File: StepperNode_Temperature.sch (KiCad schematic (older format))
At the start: 0 parts

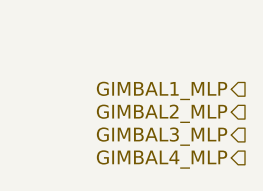
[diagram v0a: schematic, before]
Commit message: Added sheet for Stepper Motor RTD temp sensors.
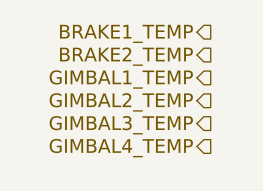
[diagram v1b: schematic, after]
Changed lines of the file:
@@
 $Descr A3 16535 11693
 encoding utf-8
-Sheet 10 17
-Title "Gimbal 4-20ma MLP Interface"
+Sheet 17 17
+Title "Stepper Motor Temperature Interface"
 Date ""
 Rev "1"
@@
 Comment4 ""
 $EndDescr
-Text HLabel 1700 1250 0    60   Output ~ 0
-GIMBAL1_MLP
-Text HLabel 1700 1350 0    60   Output ~ 0
-GIMBAL2_MLP
-Text HLabel 1700 1450 0    60   Output ~ 0
-GIMBAL3_MLP
-Text HLabel 1700 1550 0    60   Output ~ 0
-GIMBAL4_MLP
+Text HLabel 1550 1000 0    60   Output ~ 0
+BRAKE1_TEMP
+Text HLabel 1550 1100 0    60   Output ~ 0
+BRAKE2_TEMP
+Text HLabel 1550 1200 0    60   Output ~ 0
+GIMBAL1_TEMP
+Text HLabel 1550 1300 0    60   Output ~ 0
+GIMBAL2_TEMP
+Text HLabel 1550 1400 0    60   Output ~ 0
+GIMBAL3_TEMP
+Text HLabel 1550 1500 0    60   Output ~ 0
+GIMBAL4_TEMP
 $EndSCHEMATC

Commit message: Update Stepper Temp Sensor Interface
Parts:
- added C? (x6): 100nF, symbol C
- added C? (x6): 1uF, symbol C
- added D? (x6): 1N4148, symbol D
- added P? (x2): CONN_01X08_2MNT, symbol CONN_01X08_2MNT
- added U? (x6): RCV420JP, symbol RCV420JP
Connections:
- net labels added: +24V_A, BRAKE_T1_420MA, BRAKE_T2_420MA, BRAKE_T3_420MA, BRAKE_T4_420MA, GIMBAL_T1_420MA, GIMBAL_T2_420MA, GIMBAL_T3_420MA, GIMBAL_T4_420MA, GNDA
- wire segments 0 -> 60
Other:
- note added: "4-20mA for Brake and\nGimbal Temp"
- note added: "4-20mA for Gimbal Temp"
- note added: "Original Author: SafetyLok"
- note added: "rLoop - Stepper Node\n4-20mA Temp Sensor IF\n"

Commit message: Remove Gimbal Functions
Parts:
- removed C? (x4): 100nF, symbol C
- removed C? (x4): 1uF, symbol C
- removed D? (x4): 1N4148, symbol D
- removed P?: CONN_01X08_2MNT, symbol CONN_01X08_2MNT
- removed U? (x4): RCV420JP, symbol RCV420JP
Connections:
- net labels removed: GIMBAL1_TEMP, GIMBAL2_TEMP, GIMBAL3_TEMP, GIMBAL4_TEMP, GIMBAL_T1_420MA, GIMBAL_T2_420MA, GIMBAL_T3_420MA, GIMBAL_T4_420MA
- wire segments 60 -> 20
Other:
- note removed: "4-20mA for Brake and\nGimbal Temp"
- moved on the sheet: U?

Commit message: Update DAC's and routed gimbal position to MCU direct.
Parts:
- removed C? (x2): 100nF, symbol C
- removed C? (x2): 1uF, symbol C
- removed U? (x2): RCV420JP, symbol RCV420JP
- added C? (x2): C_100nF_50V, RLOOP_FOOTPRINTS:rLoop_C_0603, symbol C_100nF_50V
- added C? (x2): C_1uF_50V, RLOOP_FOOTPRINTS:rLoop_C_0603, symbol C_1uF_50V
- added U? (x2): RCV420JP, symbol RCV420JP
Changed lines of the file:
@@
 Original Author: SafetyLok
-$Comp
-L RCV420JP U?
-U 1 1 575668D5
-P 6900 2850
-F 0 "U?" H 6950 2950 60  0000 C CNN
-F 1 "RCV420JP" H 6900 1650 60  0000 C CNN
-F 2 "" H 6900 2850 60  0000 C CNN
-F 3 "" H 6900 2850 60  0000 C CNN
-	1    6900 2850
-	-1   0    0    -1
-$EndComp
 $Comp
 L +24V_A #PWR?
@@
 	5600 3350 5400 3350
 $Comp
-L C C?
-U 1 1 575669A6
-P 5150 4050
-F 0 "C?" H 5175 4150 50  0000 L CNN
-F 1 "100nF" H 5175 3950 50  0000 L CNN
-F 2 "" H 5188 3900 50  0000 C CNN
-F 3 "" H 5150 4050 50  0000 C CNN
-	1    5150 4050
-	1    0    0    -1
-$EndComp
-$Comp
-L C C?
-U 1 1 57566A33
-P 5450 4050
-F 0 "C?" H 5475 4150 50  0000 L CNN
-F 1 "1uF" H 5475 3950 50  0000 L CNN
-F 2 "" H 5488 3900 50  0000 C CNN
-F 3 "" H 5450 4050 50  0000 C CNN
-	1    5450 4050
-	1    0    0    -1
-$EndComp
-$Comp
 L GNDA #PWR?
 U 1 1 57566A6C
@@
 $Comp
 L GNDA #PWR?
-U 1 1 57566A84
-P 5150 4200
-F 0 "#PWR?" H 5150 3950 50  0001 C CNN
-F 1 "GNDA" H 5150 4050 50  0000 C CNN
-F 2 "" H 5150 4200 50  0000 C CNN
-F 3 "" H 5150 4200 50  0000 C CNN
-	1    5150 4200
-	1    0    0    -1
-$EndComp
-$Comp
-L GNDA #PWR?
 U 1 1 57566A8F
-P 5450 4200
-F 0 "#PWR?" H 5450 3950 50  0001 C CNN
-F 1 "GNDA" H 5450 4050 50  0000 C CNN
-F 2 "" H 5450 4200 50  0000 C CNN
-F 3 "" H 5450 4200 50  0000 C CNN
-	1    5450 4200
-	1    0    0    -1
-$EndComp
-$Comp
-L +24V_A #PWR?
-U 1 1 57566A9A
-P 5150 3900
-F 0 "#PWR?" H 5150 3750 50  0001 C CNN
-F 1 "+24V_A" H 5150 4040 50  0000 C CNN
-F 2 "" H 5150 3900 60  0000 C CNN
-F 3 "" H 5150 3900 60  0000 C CNN
-	1    5150 3900
-	-1   0    0    -1
+P 5100 4200
+F 0 "#PWR?" H 5100 3950 50  0001 C CNN
+F 1 "GNDA" H 5100 4050 50  0000 C CNN
+F 2 "" H 5100 4200 50  0000 C CNN
+F 3 "" H 5100 4200 50  0000 C CNN
+	1    5100 4200
+	1    0    0    -1
 $EndComp
 $Comp
 L +24V_A #PWR?
 U 1 1 57566AA5
-P 5450 3900
-F 0 "#PWR?" H 5450 3750 50  0001 C CNN
-F 1 "+24V_A" H 5450 4040 50  0000 C CNN
-F 2 "" H 5450 3900 60  0000 C CNN
-F 3 "" H 5450 3900 60  0000 C CNN
-	1    5450 3900
+P 5100 3900
+F 0 "#PWR?" H 5100 3750 50  0001 C CNN
+F 1 "+24V_A" H 5100 4040 50  0000 C CNN
+F 2 "" H 5100 3900 60  0000 C CNN
+F 3 "" H 5100 3900 60  0000 C CNN
+	1    5100 3900
 	-1   0    0    -1
 $EndComp
@@
 BRAKE2_TEMP
 $Comp
-L RCV420JP U?
-U 1 1 57568DC3
-P 6900 5200
-F 0 "U?" H 6950 5300 60  0000 C CNN
-F 1 "RCV420JP" H 6900 4000 60  0000 C CNN
-F 2 "" H 6900 5200 60  0000 C CNN
-F 3 "" H 6900 5200 60  0000 C CNN
-	1    6900 5200
-	-1   0    0    -1
-$EndComp
-$Comp
 L +24V_A #PWR?
 U 1 1 57568DC9
@@
 	5600 5700 5400 5700
 $Comp
-L C C?
-U 1 1 57568DD2
-P 5150 6400
-F 0 "C?" H 5175 6500 50  0000 L CNN
-F 1 "100nF" H 5175 6300 50  0000 L CNN
-F 2 "" H 5188 6250 50  0000 C CNN
-F 3 "" H 5150 6400 50  0000 C CNN
-	1    5150 6400
-	1    0    0    -1
-$EndComp
-$Comp
-L C C?
-U 1 1 57568DD8
-P 5450 6400
-F 0 "C?" H 5475 6500 50  0000 L CNN
-F 1 "1uF" H 5475 6300 50  0000 L CNN
-F 2 "" H 5488 6250 50  0000 C CNN
-F 3 "" H 5450 6400 50  0000 C CNN
-	1    5450 6400
-	1    0    0    -1
-$EndComp
-$Comp
 L GNDA #PWR?
 U 1 1 57568DDE
@@
 	1    6550 6600
 	1    0    0    -1
-$EndComp
-$Comp
-L GNDA #PWR?
-U 1 1 57568DE4
-P 5150 6550
-F 0 "#PWR?" H 5150 6300 50  0001 C CNN
-F 1 "GNDA" H 5150 6400 50  0000 C CNN
-F 2 "" H 5150 6550 50  0000 C CNN
-F 3 "" H 5150 6550 50  0000 C CNN
-	1    5150 6550
-	1    0    0    -1
-$EndComp
-$Comp
-L GNDA #PWR?
-U 1 1 57568DEA
-P 5450 6550
-F 0 "#PWR?" H 5450 6300 50  0001 C CNN
-F 1 "GNDA" H 5450 6400 50  0000 C CNN
-F 2 "" H 5450 6550 50  0000 C CNN
-F 3 "" H 5450 6550 50  0000 C CNN
-	1    5450 6550
-	1    0    0    -1
-$EndComp
-$Comp
-L +24V_A #PWR?
-U 1 1 57568DF0
-P 5150 6250
-F 0 "#PWR?" H 5150 6100 50  0001 C CNN
-F 1 "+24V_A" H 5150 6390 50  0000 C CNN
-F 2 "" H 5150 6250 60  0000 C CNN
-F 3 "" H 5150 6250 60  0000 C CNN
-	1    5150 6250
-	-1   0    0    -1
-$EndComp
-$Comp
-L +24V_A #PWR?
-U 1 1 57568DF6
-P 5450 6250
-F 0 "#PWR?" H 5450 6100 50  0001 C CNN
-F 1 "+24V_A" H 5450 6390 50  0000 C CNN
-F 2 "" H 5450 6250 60  0000 C CNN
-F 3 "" H 5450 6250 60  0000 C CNN
-	1    5450 6250
-	-1   0    0    -1
 $EndComp
 Wire Wire Line
@@
 Text Label 7250 5900 0    60   ~ 0
 BRAKE_T2_420MA
+$Comp
+L RCV420JP U?
+U 1 1 575A3554
+P 6900 2850
+F 0 "U?" H 6950 2950 60  0000 C CNN
+F 1 "RCV420JP" H 6900 1650 60  0000 C CNN
+F 2 "" H 6900 2850 60  0000 C CNN
+F 3 "" H 6900 2850 60  0000 C CNN
+	1    6900 2850
+	-1   0    0    -1
+$EndComp
+$Comp
+L RCV420JP U?
+U 1 1 575A3707
+P 6900 5200
+F 0 "U?" H 6950 5300 60  0000 C CNN
+F 1 "RCV420JP" H 6900 4000 60  0000 C CNN
+F 2 "" H 6900 5200 60  0000 C CNN
+F 3 "" H 6900 5200 60  0000 C CNN
+	1    6900 5200
+	-1   0    0    -1
+$EndComp
+$Comp
+L GNDA #PWR?
+U 1 1 575A39DB
+P 4400 4200
+F 0 "#PWR?" H 4400 3950 50  0001 C CNN
+F 1 "GNDA" H 4400 4050 50  0000 C CNN
+F 2 "" H 4400 4200 50  0000 C CNN
+F 3 "" H 4400 4200 50  0000 C CNN
+	1    4400 4200
+	1    0    0    -1
+$EndComp
+$Comp
+L +24V_A #PWR?
+U 1 1 575A39E1
+P 4400 3900
+F 0 "#PWR?" H 4400 3750 50  0001 C CNN
+F 1 "+24V_A" H 4400 4040 50  0000 C CNN
+F 2 "" H 4400 3900 60  0000 C CNN
+F 3 "" H 4400 3900 60  0000 C CNN
+	1    4400 3900
+	-1   0    0    -1
+$EndComp
+$Comp
+L C_100nF_50V C?
+U 1 1 575A39E7
+P 4400 4050
+F 0 "C?" H 4425 4150 50  0000 L CNN
+F 1 "C_100nF_50V" H 4425 3950 50  0000 L CNN
+F 2 "RLOOP_FOOTPRINTS:rLoop_C_0603" H 4438 3900 50  0001 C CNN
+F 3 "" H 4400 4050 50  0000 C CNN
+	1    4400 4050
+	1    0    0    -1
+$EndComp
+$Comp
+L C_1uF_50V C?
+U 1 1 575A3AB4
+P 5100 4050
+F 0 "C?" H 5125 4150 50  0000 L CNN
+F 1 "C_1uF_50V" H 5125 3950 50  0000 L CNN
+F 2 "RLOOP_FOOTPRINTS:rLoop_C_0603" H 5138 3900 50  0001 C CNN
+F 3 "" H 5100 4050 50  0000 C CNN
+	1    5100 4050
+	1    0    0    -1
+$EndComp
+$Comp
+L GNDA #PWR?
+U 1 1 575A3CB4
+P 5200 6600
+F 0 "#PWR?" H 5200 6350 50  0001 C CNN
+F 1 "GNDA" H 5200 6450 50  0000 C CNN
+F 2 "" H 5200 6600 50  0000 C CNN
+F 3 "" H 5200 6600 50  0000 C CNN
+	1    5200 6600
+	1    0    0    -1
+$EndComp
+$Comp
+L +24V_A #PWR?
+U 1 1 575A3CBA
+P 5200 6300
+F 0 "#PWR?" H 5200 6150 50  0001 C CNN
+F 1 "+24V_A" H 5200 6440 50  0000 C CNN
+F 2 "" H 5200 6300 60  0000 C CNN
+F 3 "" H 5200 6300 60  0000 C CNN
+	1    5200 6300
+	-1   0    0    -1
+$EndComp
+$Comp
+L GNDA #PWR?
+U 1 1 575A3CC0
+P 4500 6600
+F 0 "#PWR?" H 4500 6350 50  0001 C CNN
+F 1 "GNDA" H 4500 6450 50  0000 C CNN
+F 2 "" H 4500 6600 50  0000 C CNN
+F 3 "" H 4500 6600 50  0000 C CNN
+	1    4500 6600
+	1    0    0    -1
+$EndComp
+$Comp
+L +24V_A #PWR?
+U 1 1 575A3CC6
+P 4500 6300
+F 0 "#PWR?" H 4500 6150 50  0001 C CNN
+F 1 "+24V_A" H 4500 6440 50  0000 C CNN
+F 2 "" H 4500 6300 60  0000 C CNN
+F 3 "" H 4500 6300 60  0000 C CNN
+	1    4500 6300
+	-1   0    0    -1
+$EndComp
+$Comp
+L C_100nF_50V C?
+U 1 1 575A3CCC
+P 4500 6450
+F 0 "C?" H 4525 6550 50  0000 L CNN
+F 1 "C_100nF_50V" H 4525 6350 50  0000 L CNN
+F 2 "RLOOP_FOOTPRINTS:rLoop_C_0603" H 4538 6300 50  0001 C CNN
+F 3 "" H 4500 6450 50  0000 C CNN
+	1    4500 6450
+	1    0    0    -1
+$EndComp
+$Comp
+L C_1uF_50V C?
+U 1 1 575A3CD2
+P 5200 6450
+F 0 "C?" H 5225 6550 50  0000 L CNN
+F 1 "C_1uF_50V" H 5225 6350 50  0000 L CNN
+F 2 "RLOOP_FOOTPRINTS:rLoop_C_0603" H 5238 6300 50  0001 C CNN
+F 3 "" H 5200 6450 50  0000 C CNN
+	1    5200 6450
+	1    0    0    -1
+$EndComp
 $EndSCHEMATC

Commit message: First Revision -
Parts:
- removed D? (x2): 1N4148, symbol D
- removed P?: CONN_01X08_2MNT, symbol CONN_01X08_2MNT
- removed U? (x2): RCV420JP, symbol RCV420JP
- added D7, D8: BAS16,215, RLOOP_FOOTPRINTS:rLoop_SOT23, symbol BAS16,215
- added P13: TE_640456-8, RLOOP_FOOTPRINTS:rLoop_TE640456-8, symbol TE_640456-8
- added U23, U24: RCV420JP, RLOOP_FOOTPRINTS:rLoop_DIP16, symbol RCV420JP
- gave numbers to parts that had none: 4
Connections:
- net labels removed: BRAKE_T3_420MA, BRAKE_T4_420MA
- wire segments 20 -> 23

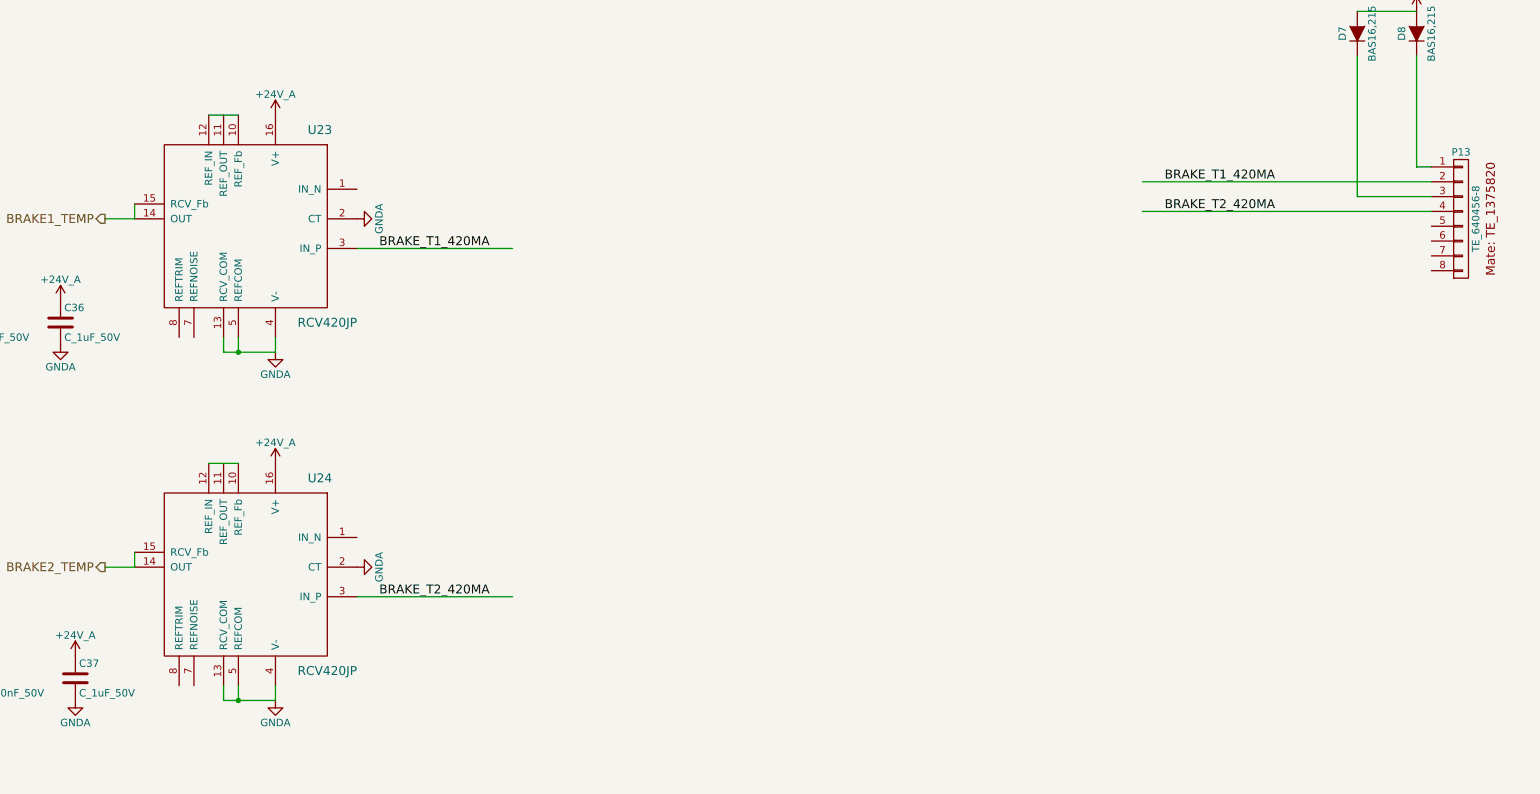
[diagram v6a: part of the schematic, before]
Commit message: Fix most ERC warnings (non-connected pins, etc)
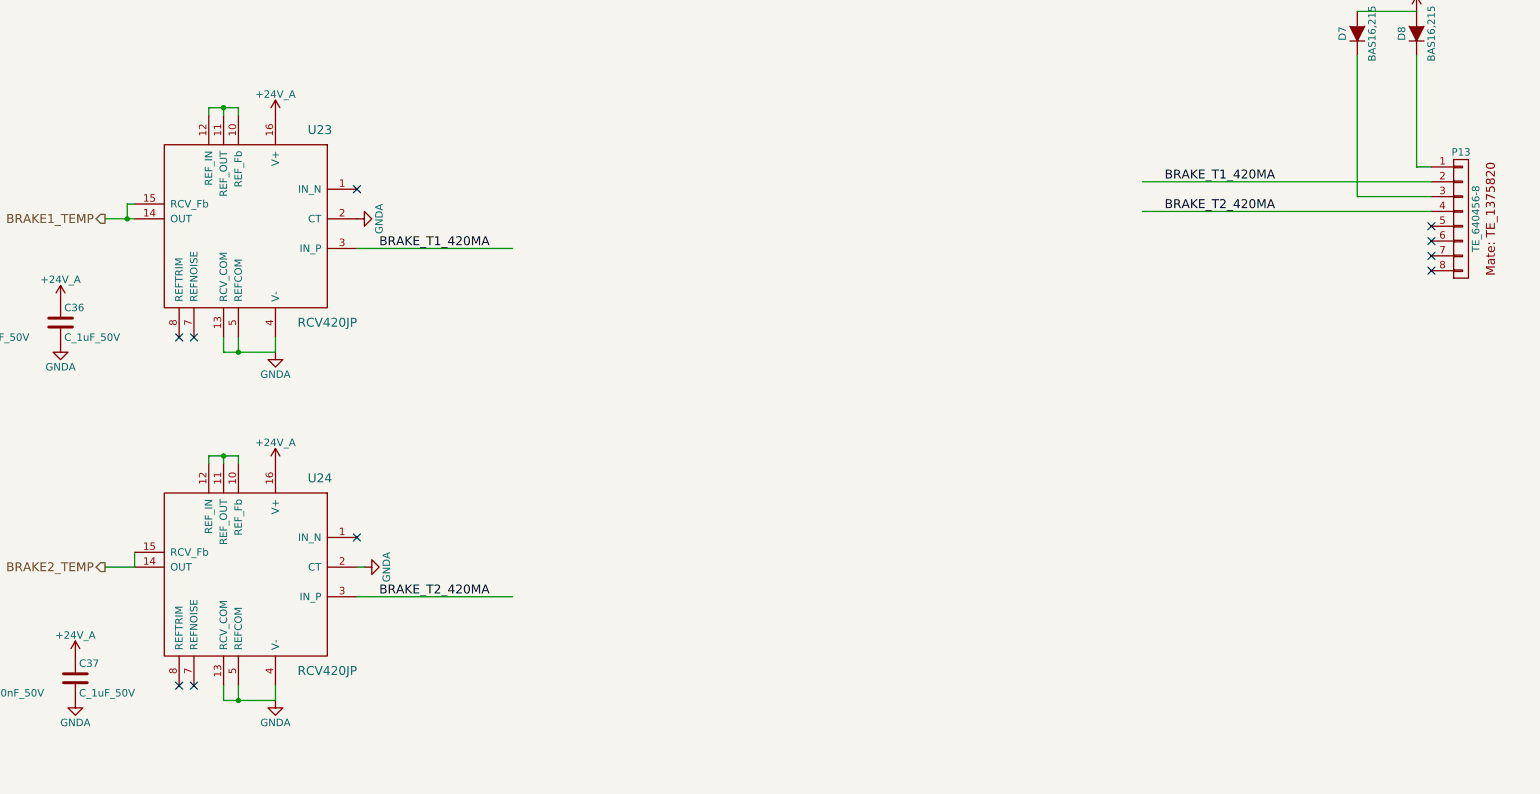
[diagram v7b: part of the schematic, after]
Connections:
- wire segments 23 -> 31
- no-connect marks 0 -> 10
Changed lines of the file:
@@
 Original Author: SafetyLok
 $Comp
-L +24V_A #PWR156
+L +24V_A #PWR0159
 U 1 1 5756693D
 P 6550 2650
-F 0 "#PWR156" H 6550 2500 50  0001 C CNN
+F 0 "#PWR0159" H 6550 2500 50  0001 C CNN
 F 1 "+24V_A" H 6550 2790 50  0000 C CNN
 F 2 "" H 6550 2650 60  0000 C CNN
@@
 $EndComp
 $Comp
-L GNDA #PWR157
+L GNDA #PWR0160
 U 1 1 57566A6C
 P 6550 4250
-F 0 "#PWR157" H 6550 4000 50  0001 C CNN
+F 0 "#PWR0160" H 6550 4000 50  0001 C CNN
 F 1 "GNDA" H 6550 4100 50  0000 C CNN
 F 2 "" H 6550 4250 50  0000 C CNN
@@
 $EndComp
 $Comp
-L GNDA #PWR153
+L GNDA #PWR0161
 U 1 1 57566A8F
 P 5100 4200
-F 0 "#PWR153" H 5100 3950 50  0001 C CNN
+F 0 "#PWR0161" H 5100 3950 50  0001 C CNN
 F 1 "GNDA" H 5100 4050 50  0000 C CNN
 F 2 "" H 5100 4200 50  0000 C CNN
@@
 $EndComp
 $Comp
-L +24V_A #PWR152
+L +24V_A #PWR0162
 U 1 1 57566AA5
 P 5100 3900
-F 0 "#PWR152" H 5100 3750 50  0001 C CNN
+F 0 "#PWR0162" H 5100 3750 50  0001 C CNN
 F 1 "+24V_A" H 5100 4040 50  0000 C CNN
 F 2 "" H 5100 3900 60  0000 C CNN
@@
 $EndComp
 $Comp
-L GNDA #PWR160
+L GNDA #PWR0163
 U 1 1 57566AD9
 P 7100 3350
-F 0 "#PWR160" H 7100 3100 50  0001 C CNN
+F 0 "#PWR0163" H 7100 3100 50  0001 C CNN
 F 1 "GNDA" H 7100 3200 50  0000 C CNN
 F 2 "" H 7100 3350 50  0000 C CNN
@@
 BRAKE_T1_420MA
 $Comp
-L +24V_A #PWR162
+L +24V_A #PWR0164
 U 1 1 57567FBD
 P 14250 1950
-F 0 "#PWR162" H 14250 1800 50  0001 C CNN
+F 0 "#PWR0164" H 14250 1800 50  0001 C CNN
 F 1 "+24V_A" H 14250 2090 50  0000 C CNN
 F 2 "" H 14250 1950 60  0000 C CNN
@@
 BRAKE2_TEMP
 $Comp
-L +24V_A #PWR158
+L +24V_A #PWR0165
 U 1 1 57568DC9
 P 6550 5000
-F 0 "#PWR158" H 6550 4850 50  0001 C CNN
+F 0 "#PWR0165" H 6550 4850 50  0001 C CNN
 F 1 "+24V_A" H 6550 5140 50  0000 C CNN
 F 2 "" H 6550 5000 60  0000 C CNN
@@
 $EndComp
 $Comp
-L GNDA #PWR159
+L GNDA #PWR0166
 U 1 1 57568DDE
 P 6550 6600
-F 0 "#PWR159" H 6550 6350 50  0001 C CNN
+F 0 "#PWR0166" H 6550 6350 50  0001 C CNN
 F 1 "GNDA" H 6550 6450 50  0000 C CNN
 F 2 "" H 6550 6600 50  0000 C CNN
@@
 $EndComp
 $Comp
-L GNDA #PWR161
+L GNDA #PWR0167
 U 1 1 57568E01
-P 7100 5700
-F 0 "#PWR161" H 7100 5450 50  0001 C CNN
-F 1 "GNDA" H 7100 5550 50  0000 C CNN
-F 2 "" H 7100 5700 50  0000 C CNN
-F 3 "" H 7100 5700 50  0000 C CNN
-	1    7100 5700
+P 7150 5700
+F 0 "#PWR0167" H 7150 5450 50  0001 C CNN
+F 1 "GNDA" H 7150 5550 50  0000 C CNN
+F 2 "" H 7150 5700 50  0000 C CNN
+F 3 "" H 7150 5700 50  0000 C CNN
+	1    7150 5700
 	0    -1   -1   0
 $EndComp
@@
 BRAKE_T2_420MA
 $Comp
-L GNDA #PWR149
+L GNDA #PWR0168
 U 1 1 575A39DB
 P 4400 4200
-F 0 "#PWR149" H 4400 3950 50  0001 C CNN
+F 0 "#PWR0168" H 4400 3950 50  0001 C CNN
 F 1 "GNDA" H 4400 4050 50  0000 C CNN
 F 2 "" H 4400 4200 50  0000 C CNN
@@
 $EndComp
 $Comp
-L +24V_A #PWR148
+L +24V_A #PWR0169
 U 1 1 575A39E1
 P 4400 3900
-F 0 "#PWR148" H 4400 3750 50  0001 C CNN
+F 0 "#PWR0169" H 4400 3750 50  0001 C CNN
 F 1 "+24V_A" H 4400 4040 50  0000 C CNN
 F 2 "" H 4400 3900 60  0000 C CNN
@@
 $EndComp
 $Comp
-L GNDA #PWR155
+L GNDA #PWR0170
 U 1 1 575A3CB4
 P 5200 6600
-F 0 "#PWR155" H 5200 6350 50  0001 C CNN
+F 0 "#PWR0170" H 5200 6350 50  0001 C CNN
 F 1 "GNDA" H 5200 6450 50  0000 C CNN
 F 2 "" H 5200 6600 50  0000 C CNN
@@
 $EndComp
 $Comp
-L +24V_A #PWR154
+L +24V_A #PWR0171
 U 1 1 575A3CBA
 P 5200 6300
-F 0 "#PWR154" H 5200 6150 50  0001 C CNN
+F 0 "#PWR0171" H 5200 6150 50  0001 C CNN
 F 1 "+24V_A" H 5200 6440 50  0000 C CNN
 F 2 "" H 5200 6300 60  0000 C CNN
@@
 $EndComp
 $Comp
-L GNDA #PWR151
+L GNDA #PWR0172
 U 1 1 575A3CC0
 P 4500 6600
-F 0 "#PWR151" H 4500 6350 50  0001 C CNN
+F 0 "#PWR0172" H 4500 6350 50  0001 C CNN
 F 1 "GNDA" H 4500 6450 50  0000 C CNN
 F 2 "" H 4500 6600 50  0000 C CNN
@@
 $EndComp
 $Comp
-L +24V_A #PWR150
+L +24V_A #PWR0173
 U 1 1 575A3CC6
 P 4500 6300
-F 0 "#PWR150" H 4500 6150 50  0001 C CNN
+F 0 "#PWR0173" H 4500 6150 50  0001 C CNN
 F 1 "+24V_A" H 4500 6440 50  0000 C CNN
 F 2 "" H 4500 6300 60  0000 C CNN
@@
 $EndComp
 Wire Wire Line
-	6300 2650 6100 2650
-Wire Wire Line
-	5600 3250 5600 3350
-Wire Wire Line
-	5600 3350 5400 3350
+	5400 3350 5600 3350
 Wire Wire Line
 	6200 4150 6200 4250
@@
 Wire Wire Line
 	12400 3300 14350 3300
-Wire Wire Line
-	6300 5000 6100 5000
 Wire Wire Line
 	5600 5600 5600 5700
@@
 	1    0    0    -1
 $EndComp
+NoConn ~ 6000 4150
+NoConn ~ 5900 4150
+Wire Wire Line
+	5600 3250 5550 3250
+Wire Wire Line
+	5550 3250 5550 3350
+Connection ~ 5550 3350
+NoConn ~ 7100 3150
+Wire Wire Line
+	6100 2650 6100 2600
+Wire Wire Line
+	6100 2600 6300 2600
+Wire Wire Line
+	6300 2600 6300 2650
+Wire Wire Line
+	6200 2650 6200 2600
+Connection ~ 6200 2600
+NoConn ~ 5900 6500
+NoConn ~ 6000 6500
+Wire Wire Line
+	6100 5000 6100 4950
+Wire Wire Line
+	6100 4950 6300 4950
+Wire Wire Line
+	6300 4950 6300 5000
+Wire Wire Line
+	6200 5000 6200 4950
+Connection ~ 6200 4950
+NoConn ~ 7100 5500
+Wire Wire Line
+	7150 5700 7100 5700
+NoConn ~ 14350 3400
+NoConn ~ 14350 3500
+NoConn ~ 14350 3600
+NoConn ~ 14350 3700
 $EndSCHEMATC
